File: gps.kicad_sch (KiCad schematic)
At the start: 8 parts, among them U700 NEO-6P, X7 Conn_Coaxial

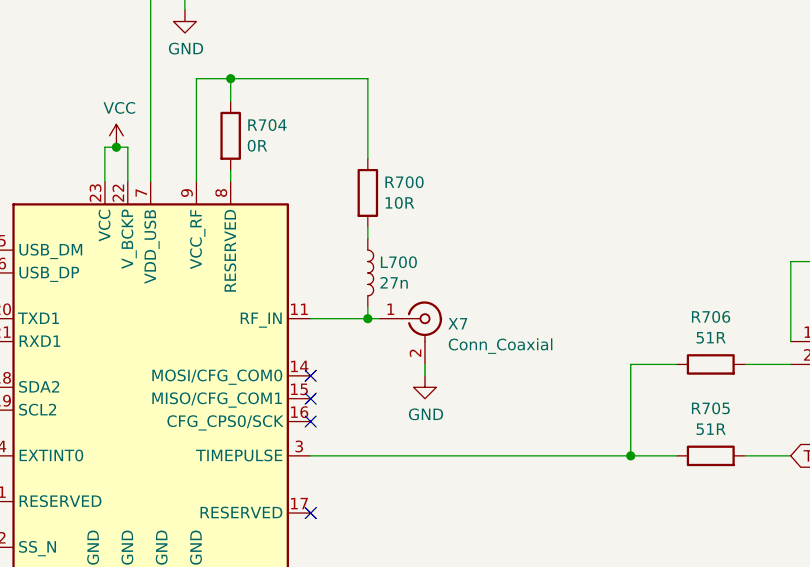
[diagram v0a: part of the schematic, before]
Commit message: Changes in BOM. Add JLCpcb Part Nr
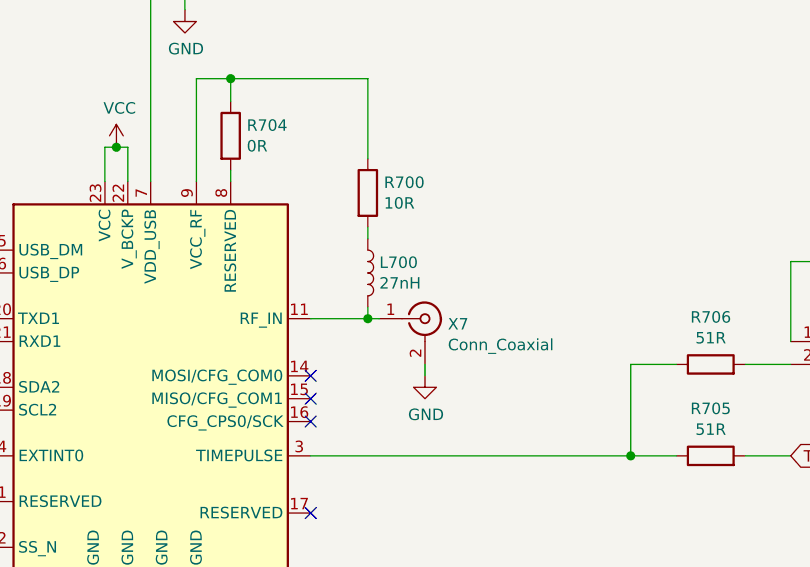
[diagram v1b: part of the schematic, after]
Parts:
- L700: value 27n -> 27nH; footprint (none) -> Inductor_SMD:L_0805_2012Metric_Pad1.15x1.40mm_HandSolder; JLCBasicPart (none) -> Extended; JLCPartNr (none) -> C56586; JLCType (none) -> MLI2012-27N(f); OriginalType (none) -> VHF201209H27NJT; Supplier (none) -> LCSC
- R700: footprint (none) -> Resistor_SMD:R_0805_2012Metric_Pad1.20x1.40mm_HandSolder; JLCBasicPart (none) -> Basic; JLCPartNr (none) -> C17415; JLCType (none) -> 0805W8F100JT5E; OriginalType (none) -> RK73H2ATTD10R0F
- R704: footprint (none) -> Resistor_SMD:R_0805_2012Metric_Pad1.20x1.40mm_HandSolder; JLCBasicPart (none) -> Basic; JLCPartNr (none) -> C17477; JLCType (none) -> 0805W8F0000T5E; OriginalType (none) -> --
- R705, R706: footprint (none) -> Resistor_SMD:R_0805_2012Metric_Pad1.20x1.40mm_HandSolder; JLCBasicPart (none) -> Basic; JLCPartNr (none) -> C17738; JLCType (none) -> 0805W8F510JT5E; OriginalType (none) -> CR0805J80510G
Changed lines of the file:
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@@
   (symbol (lib_id "power:VCC") (at 142.24 60.96 0) (unit 1)
     (in_bom yes) (on_board yes)
-    (property "Reference" "#PWR?" (id 0) (at 142.24 64.77 0)
+    (property "Reference" "#PWR0135" (id 0) (at 142.24 64.77 0)
       (effects (font (size 1.27 1.27)) hide)
     )
@@
   (symbol (lib_id "power:GND") (at 139.7 114.3 0) (unit 1)
     (in_bom yes) (on_board yes)
-    (property "Reference" "#PWR?" (id 0) (at 139.7 120.65 0)
+    (property "Reference" "#PWR0134" (id 0) (at 139.7 120.65 0)
       (effects (font (size 1.27 1.27)) hide)
     )
@@
   (symbol (lib_id "power:GND") (at 149.86 45.72 0) (unit 1)
     (in_bom yes) (on_board yes)
-    (property "Reference" "#PWR?" (id 0) (at 149.86 52.07 0)
+    (property "Reference" "#PWR0138" (id 0) (at 149.86 52.07 0)
       (effects (font (size 1.27 1.27)) hide)
     )
@@
   (symbol (lib_id "power:GND") (at 176.53 86.36 0) (unit 1)
     (in_bom yes) (on_board yes)
-    (property "Reference" "#PWR?" (id 0) (at 176.53 92.71 0)
+    (property "Reference" "#PWR0137" (id 0) (at 176.53 92.71 0)
       (effects (font (size 1.27 1.27)) hide)
     )
@@
   (symbol (lib_id "power:GND") (at 222.25 74.93 0) (unit 1)
     (in_bom yes) (on_board yes)
-    (property "Reference" "#PWR?" (id 0) (at 222.25 81.28 0)
+    (property "Reference" "#PWR0136" (id 0) (at 222.25 81.28 0)
       (effects (font (size 1.27 1.27)) hide)
     )
@@
       (effects (font (size 1.27 1.27)) (justify left))
     )
-    (property "Value" "27n" (id 1) (at 171.4501 76.0793 0)
-      (effects (font (size 1.27 1.27)) (justify left))
-    )
-    (property "Footprint" "" (id 2) (at 170.18 74.93 0)
+    (property "Value" "27nH" (id 1) (at 171.4501 76.0793 0)
+      (effects (font (size 1.27 1.27)) (justify left))
+    )
+    (property "Footprint" "Inductor_SMD:L_0805_2012Metric_Pad1.15x1.40mm_HandSolder" (id 2) (at 170.18 74.93 0)
       (effects (font (size 1.27 1.27)) hide)
     )
@@
       (effects (font (size 1.27 1.27)) hide)
     )
+    (property "JLCBasicPart" "Extended" (id 4) (at 170.18 74.93 0)
+      (effects (font (size 1.27 1.27)) hide)
+    )
+    (property "JLCPartNr" "C56586" (id 5) (at 170.18 74.93 0)
+      (effects (font (size 1.27 1.27)) hide)
+    )
+    (property "JLCType" "MLI2012-27N(f)" (id 6) (at 170.18 74.93 0)
+      (effects (font (size 1.27 1.27)) hide)
+    )
+    (property "OriginalType" "VHF201209H27NJT " (id 7) (at 170.18 74.93 0)
+      (effects (font (size 1.27 1.27)) hide)
+    )
+    (property "Supplier" "LCSC " (id 8) (at 170.18 74.93 0)
+      (effects (font (size 1.27 1.27)) hide)
+    )
     (pin "1")
     (pin "2")
@@
       (effects (font (size 1.27 1.27)) (justify left))
     )
-    (property "Footprint" "" (id 2) (at 153.162 59.69 90)
+    (property "Footprint" "Resistor_SMD:R_0805_2012Metric_Pad1.20x1.40mm_HandSolder" (id 2) (at 153.162 59.69 90)
       (effects (font (size 1.27 1.27)) hide)
     )
@@
       (effects (font (size 1.27 1.27)) hide)
     )
+    (property "JLCBasicPart" "Basic" (id 4) (at 154.94 59.69 0)
+      (effects (font (size 1.27 1.27)) hide)
+    )
+    (property "JLCPartNr" "C17477" (id 5) (at 154.94 59.69 0)
+      (effects (font (size 1.27 1.27)) hide)
+    )
+    (property "JLCType" "0805W8F0000T5E" (id 6) (at 154.94 59.69 0)
+      (effects (font (size 1.27 1.27)) hide)
+    )
+    (property "OriginalType" "--" (id 7) (at 154.94 59.69 0)
+      (effects (font (size 1.27 1.27)) hide)
+    )
     (pin "1")
     (pin "2")
@@
       (effects (font (size 1.27 1.27)) (justify left))
     )
-    (property "Footprint" "" (id 2) (at 168.402 66.04 90)
+    (property "Footprint" "Resistor_SMD:R_0805_2012Metric_Pad1.20x1.40mm_HandSolder" (id 2) (at 168.402 66.04 90)
       (effects (font (size 1.27 1.27)) hide)
     )
     (property "Datasheet" "~" (id 3) (at 170.18 66.04 0)
+      (effects (font (size 1.27 1.27)) hide)
+    )
+    (property "JLCBasicPart" "Basic" (id 4) (at 170.18 66.04 0)
+      (effects (font (size 1.27 1.27)) hide)
+    )
+    (property "JLCPartNr" "C17415" (id 5) (at 170.18 66.04 0)
+      (effects (font (size 1.27 1.27)) hide)
+    )
+    (property "JLCType" "0805W8F100JT5E" (id 6) (at 170.18 66.04 0)
+      (effects (font (size 1.27 1.27)) hide)
+    )
+    (property "OriginalType" "RK73H2ATTD10R0F " (id 7) (at 170.18 66.04 0)
       (effects (font (size 1.27 1.27)) hide)
     )
@@
     (property "Reference" "R706" (id 0) (at 208.28 79.8576 90))
     (property "Value" "51R" (id 1) (at 208.28 82.169 90))
-    (property "Footprint" "" (id 2) (at 208.28 86.868 90)
+    (property "Footprint" "Resistor_SMD:R_0805_2012Metric_Pad1.20x1.40mm_HandSolder" (id 2) (at 208.28 86.868 90)
       (effects (font (size 1.27 1.27)) hide)
     )
     (property "Datasheet" "~" (id 3) (at 208.28 85.09 0)
+      (effects (font (size 1.27 1.27)) hide)
+    )
+    (property "JLCBasicPart" "Basic" (id 4) (at 208.28 85.09 0)
+      (effects (font (size 1.27 1.27)) hide)
+    )
+    (property "JLCPartNr" "C17738" (id 5) (at 208.28 85.09 0)
+      (effects (font (size 1.27 1.27)) hide)
+    )
+    (property "JLCType" "0805W8F510JT5E" (id 6) (at 208.28 85.09 0)
+      (effects (font (size 1.27 1.27)) hide)
+    )
+    (property "OriginalType" "CR0805J80510G " (id 7) (at 208.28 85.09 0)
       (effects (font (size 1.27 1.27)) hide)
     )
@@
     (property "Reference" "R705" (id 0) (at 208.28 90.0176 90))
     (property "Value" "51R" (id 1) (at 208.28 92.329 90))
-    (property "Footprint" "" (id 2) (at 208.28 97.028 90)
+    (property "Footprint" "Resistor_SMD:R_0805_2012Metric_Pad1.20x1.40mm_HandSolder" (id 2) (at 208.28 97.028 90)
       (effects (font (size 1.27 1.27)) hide)
     )
@@
       (effects (font (size 1.27 1.27)) hide)
     )
+    (property "JLCBasicPart" "Basic" (id 4) (at 208.28 95.25 0)
+      (effects (font (size 1.27 1.27)) hide)
+    )
+    (property "JLCPartNr" "C17738" (id 5) (at 208.28 95.25 0)
+      (effects (font (size 1.27 1.27)) hide)
+    )
+    (property "JLCType" "0805W8F510JT5E" (id 6) (at 208.28 95.25 0)
+      (effects (font (size 1.27 1.27)) hide)
+    )
+    (property "OriginalType" "CR0805J80510G " (id 7) (at 208.28 95.25 0)
+      (effects (font (size 1.27 1.27)) hide)
+    )

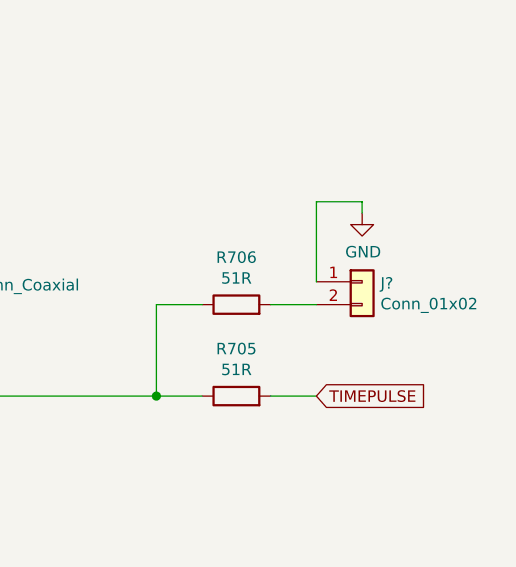
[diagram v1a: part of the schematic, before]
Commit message: working on BOM. Small Fixes in Schematics
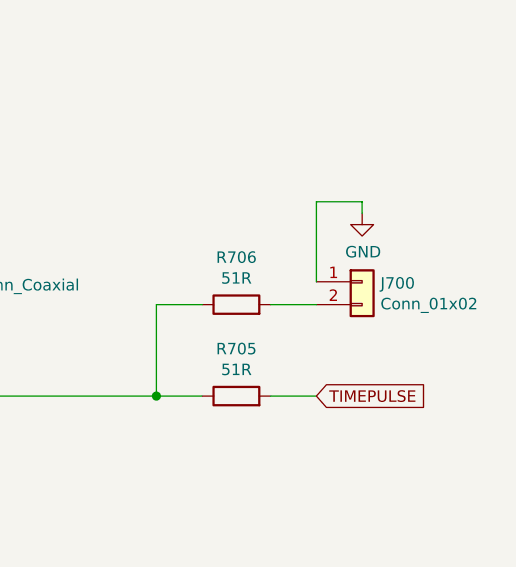
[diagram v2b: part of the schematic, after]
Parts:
- gave numbers to parts that had none: 1
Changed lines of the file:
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@@
   (symbol (lib_id "Connector_Generic:Conn_01x02") (at 222.25 82.55 0) (unit 1)
     (in_bom yes) (on_board yes)
-    (property "Reference" "J?" (id 0) (at 224.2821 82.7214 0)
+    (property "Reference" "J700" (id 0) (at 224.2821 82.7214 0)
       (effects (font (size 1.27 1.27)) (justify left))
     )

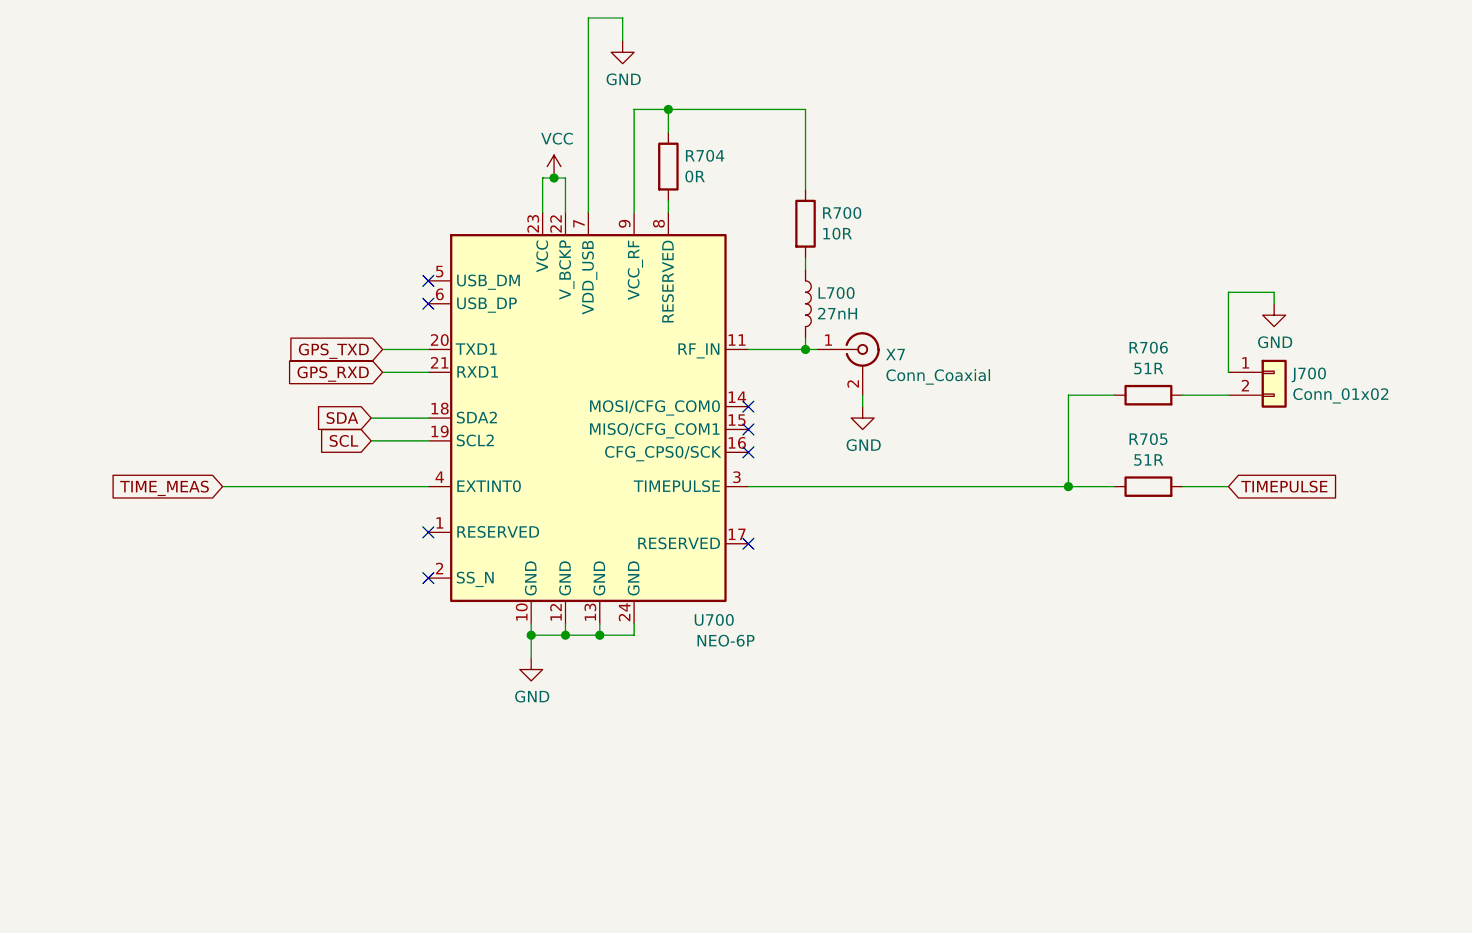
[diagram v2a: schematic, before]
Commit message: Footprints assigned. Testpoints added
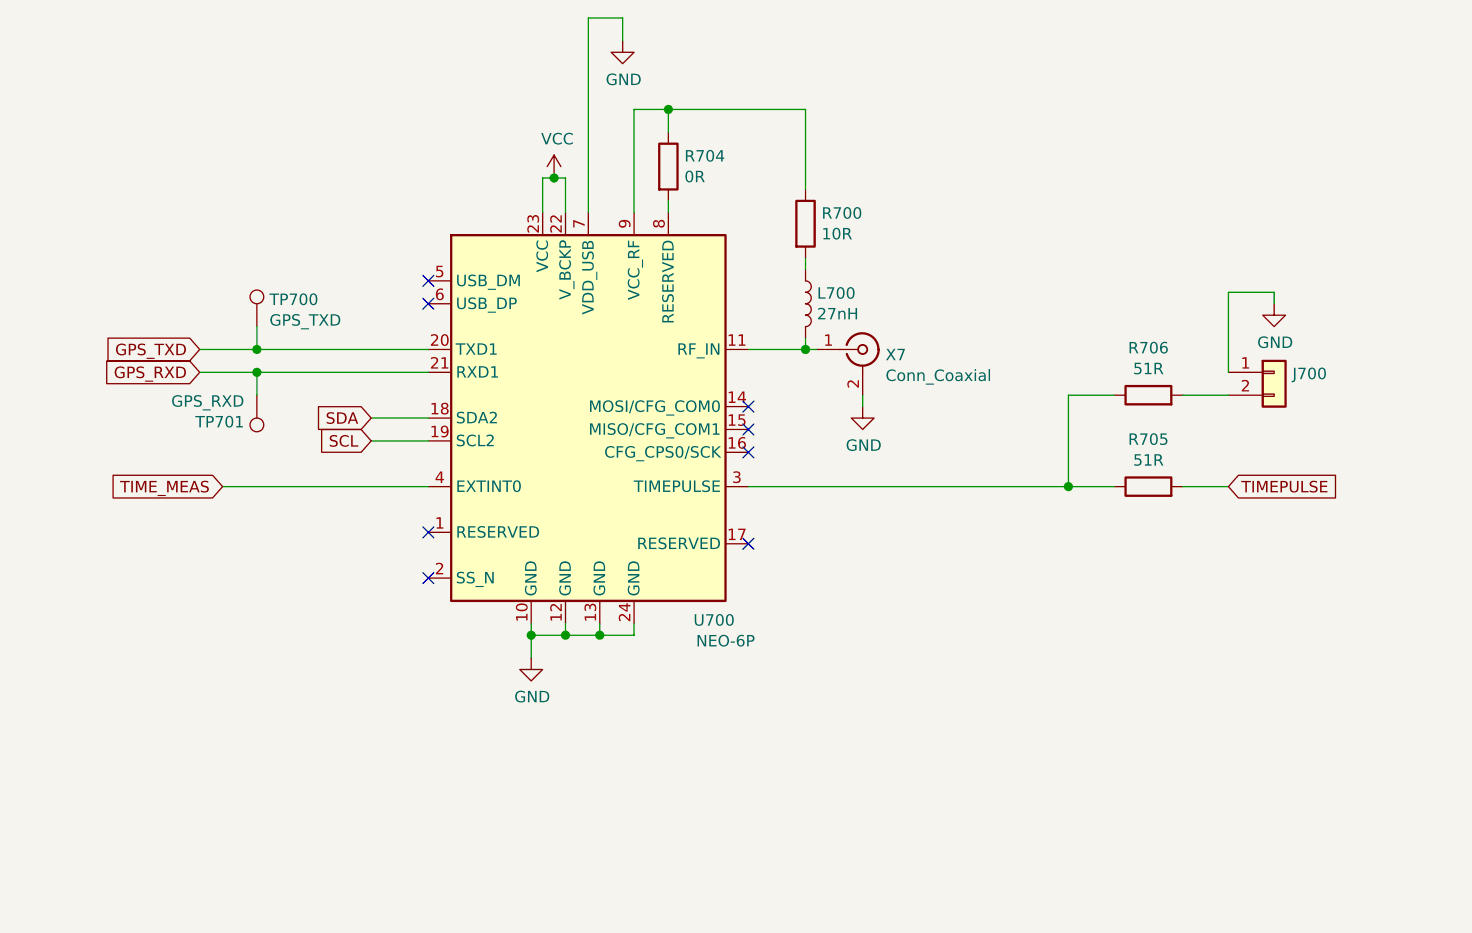
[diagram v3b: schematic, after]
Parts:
- added TP700: GPS_TXD, TestPoint:TestPoint_THTPad_1.5x1.5mm_Drill0.7mm, symbol Connector:TestPoint
- added TP701: GPS_RXD, TestPoint:TestPoint_THTPad_1.5x1.5mm_Drill0.7mm, symbol Connector:TestPoint
- J700: footprint (none) -> Connector_PinHeader_2.54mm:PinHeader_1x02_P2.54mm_Vertical; now left out of the parts list
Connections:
- net GPS_RXD: now also TP701.1
- net GPS_TXD: now also TP700.1
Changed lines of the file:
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@@
 (kicad_sch (version 20210406) (generator eeschema)
   (paper "A4")
+  (junction (at 109.22 80.01) (diameter 1.016) (color 0 0 0 0))
+  (junction (at 109.22 82.55) (diameter 1.016) (color 0 0 0 0))
   (junction (at 139.7 111.76) (diameter 1.016) (color 0 0 0 0))
   (junction (at 142.24 60.96) (diameter 1.016) (color 0 0 0 0))
@@
   (no_connect (at 163.83 91.44))
   (no_connect (at 163.83 101.6))
+  (wire (pts (xy 102.87 80.01) (xy 109.22 80.01))
+    (stroke (width 0) (type solid) (color 0 0 0 0))
+  )
+  (wire (pts (xy 102.87 82.55) (xy 109.22 82.55))
+    (stroke (width 0) (type solid) (color 0 0 0 0))
+  )
   (wire (pts (xy 105.41 95.25) (xy 128.27 95.25))
     (stroke (width 0) (type solid) (color 0 0 0 0))
   )
+  (wire (pts (xy 109.22 77.47) (xy 109.22 80.01))
+    (stroke (width 0) (type solid) (color 0 0 0 0))
+  )
+  (wire (pts (xy 109.22 80.01) (xy 128.27 80.01))
+    (stroke (width 0) (type solid) (color 0 0 0 0))
+  )
+  (wire (pts (xy 109.22 82.55) (xy 109.22 85.09))
+    (stroke (width 0) (type solid) (color 0 0 0 0))
+  )
+  (wire (pts (xy 109.22 82.55) (xy 128.27 82.55))
+    (stroke (width 0) (type solid) (color 0 0 0 0))
+  )
   (wire (pts (xy 121.92 87.63) (xy 128.27 87.63))
     (stroke (width 0) (type solid) (color 0 0 0 0))
@@
     (stroke (width 0) (type solid) (color 0 0 0 0))
   )
-  (wire (pts (xy 123.19 80.01) (xy 128.27 80.01))
-    (stroke (width 0) (type solid) (color 0 0 0 0))
-  )
-  (wire (pts (xy 123.19 82.55) (xy 128.27 82.55))
-    (stroke (width 0) (type solid) (color 0 0 0 0))
-  )
   (wire (pts (xy 139.7 110.49) (xy 139.7 111.76))
     (stroke (width 0) (type solid) (color 0 0 0 0))
@@
   (wire (pts (xy 222.25 73.66) (xy 222.25 74.93))
     (stroke (width 0) (type solid) (color 0 0 0 0))
+  )
+  (global_label "GPS_TXD" (shape input) (at 102.87 80.01 180)
+    (effects (font (size 1.27 1.27)) (justify right))
+    (property "Intersheet References" "${INTERSHEET_REFS}" (id 0) (at 90.7686 79.9306 0)
+      (effects (font (size 1.27 1.27)) (justify right) hide)
+    )
+  )
+  (global_label "GPS_RXD" (shape input) (at 102.87 82.55 180)
+    (effects (font (size 1.27 1.27)) (justify right))
+    (property "Intersheet References" "${INTERSHEET_REFS}" (id 0) (at 90.4662 82.4706 0)
+      (effects (font (size 1.27 1.27)) (justify right) hide)
+    )
   )
   (global_label "TIME_MEAS" (shape input) (at 105.41 95.25 180)
@@
     )
   )
-  (global_label "GPS_TXD" (shape input) (at 123.19 80.01 180)
-    (effects (font (size 1.27 1.27)) (justify right))
-    (property "Intersheet References" "${INTERSHEET_REFS}" (id 0) (at 111.0886 79.9306 0)
-      (effects (font (size 1.27 1.27)) (justify right) hide)
-    )
-  )
-  (global_label "GPS_RXD" (shape input) (at 123.19 82.55 180)
-    (effects (font (size 1.27 1.27)) (justify right))
-    (property "Intersheet References" "${INTERSHEET_REFS}" (id 0) (at 110.7862 82.4706 0)
-      (effects (font (size 1.27 1.27)) (justify right) hide)
-    )
-  )
   (global_label "TIMEPULSE" (shape input) (at 217.17 95.25 0)
     (effects (font (size 1.27 1.27)) (justify left))
@@
     (pin "1")
   )
+  (symbol (lib_id "Connector:TestPoint") (at 109.22 77.47 0) (unit 1)
+    (in_bom no) (on_board yes)
+    (property "Reference" "TP700" (id 0) (at 110.6171 74.4791 0)
+      (effects (font (size 1.27 1.27)) (justify left))
+    )
+    (property "Value" "GPS_TXD" (id 1) (at 110.6171 76.7778 0)
+      (effects (font (size 1.27 1.27)) (justify left))
+    )
+    (property "Footprint" "TestPoint:TestPoint_THTPad_1.5x1.5mm_Drill0.7mm" (id 2) (at 114.3 77.47 0)
+      (effects (font (size 1.27 1.27)) hide)
+    )
+    (property "Datasheet" "~" (id 3) (at 114.3 77.47 0)
+      (effects (font (size 1.27 1.27)) hide)
+    )
+    (pin "1")
+  )
+  (symbol (lib_id "Connector:TestPoint") (at 109.22 85.09 180) (unit 1)
+    (in_bom no) (on_board yes)
+    (property "Reference" "TP701" (id 0) (at 107.8229 88.0809 0)
+      (effects (font (size 1.27 1.27)) (justify left))
+    )
+    (property "Value" "GPS_RXD" (id 1) (at 107.8229 85.7822 0)
+      (effects (font (size 1.27 1.27)) (justify left))
+    )
+    (property "Footprint" "TestPoint:TestPoint_THTPad_1.5x1.5mm_Drill0.7mm" (id 2) (at 104.14 85.09 0)
+      (effects (font (size 1.27 1.27)) hide)
+    )
+    (property "Datasheet" "~" (id 3) (at 104.14 85.09 0)
+      (effects (font (size 1.27 1.27)) hide)
+    )
+    (pin "1")
+  )
   (symbol (lib_id "power:GND") (at 139.7 114.3 0) (unit 1)
     (in_bom yes) (on_board yes)
@@
   )
   (symbol (lib_id "Connector_Generic:Conn_01x02") (at 222.25 82.55 0) (unit 1)
-    (in_bom yes) (on_board yes)
+    (in_bom no) (on_board yes)
     (property "Reference" "J700" (id 0) (at 224.2821 82.7214 0)
       (effects (font (size 1.27 1.27)) (justify left))
     )
     (property "Value" "Conn_01x02" (id 1) (at 224.2821 85.0201 0)
-      (effects (font (size 1.27 1.27)) (justify left))
-    )
-    (property "Footprint" "" (id 2) (at 222.25 82.55 0)
-      (effects (font (size 1.27 1.27)) hide)
-    )
+      (effects (font (size 1.27 1.27)) (justify left) hide)
+    )
+    (property "Footprint" "Connector_PinHeader_2.54mm:PinHeader_1x02_P2.54mm_Vertical" (id 2) (at 222.25 82.55 0)
+      (effects (font (size 1.27 1.27)) hide)
+    )
